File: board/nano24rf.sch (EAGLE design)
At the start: 18 parts

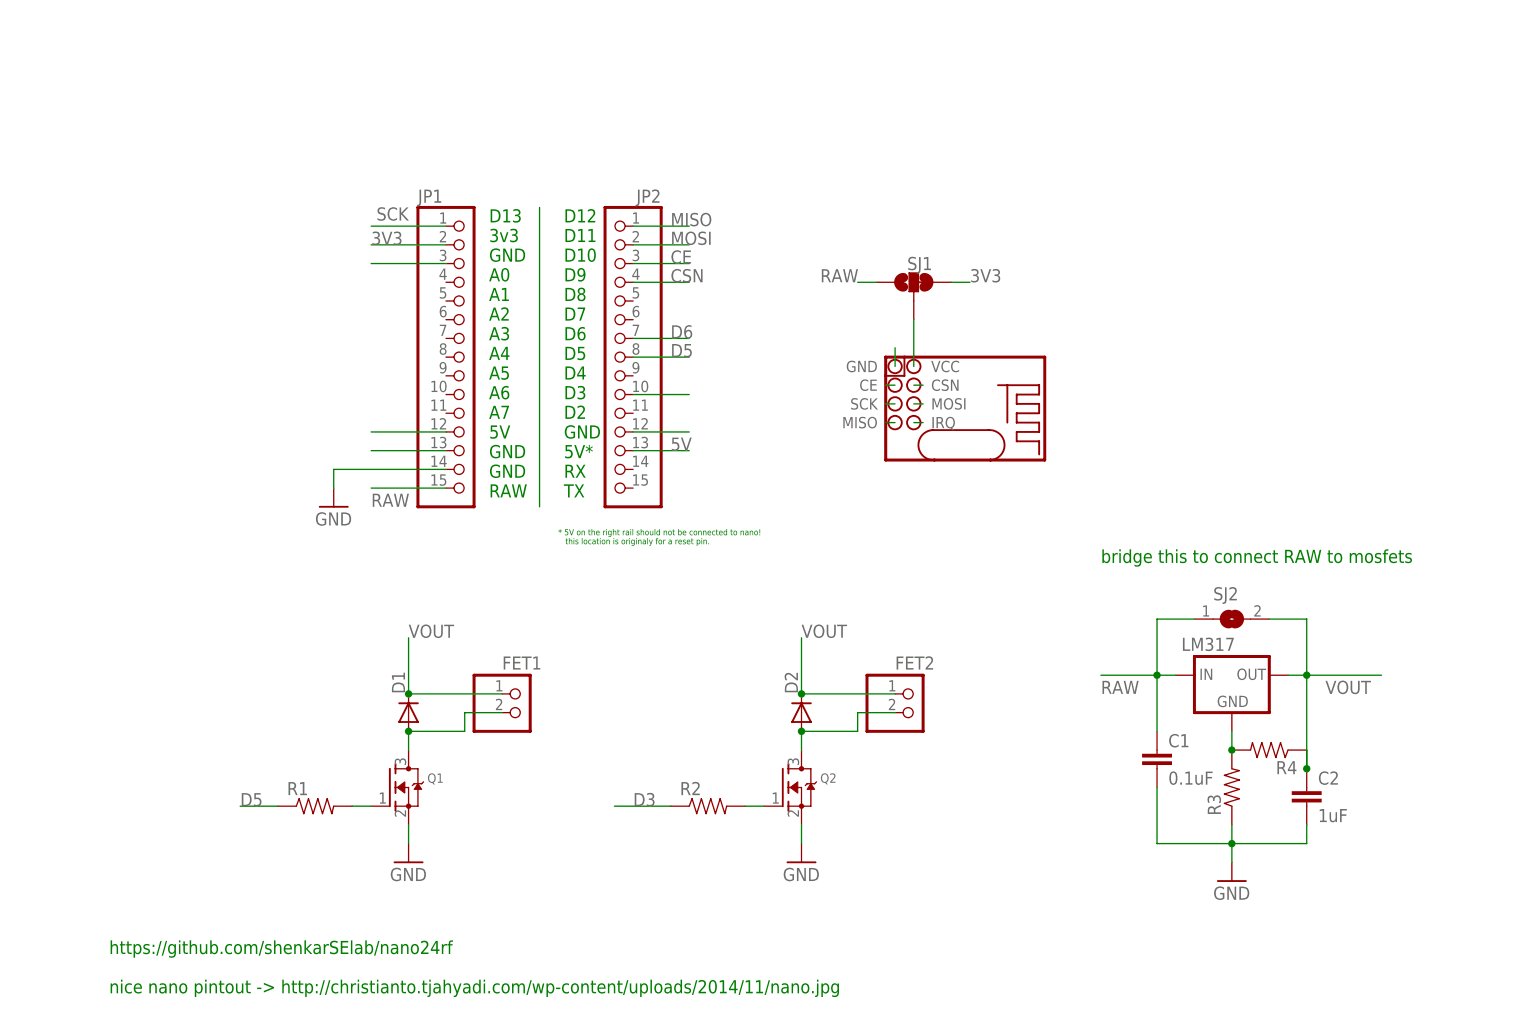
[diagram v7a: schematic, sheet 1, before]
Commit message: removed lm317 and placed msfets on bottom
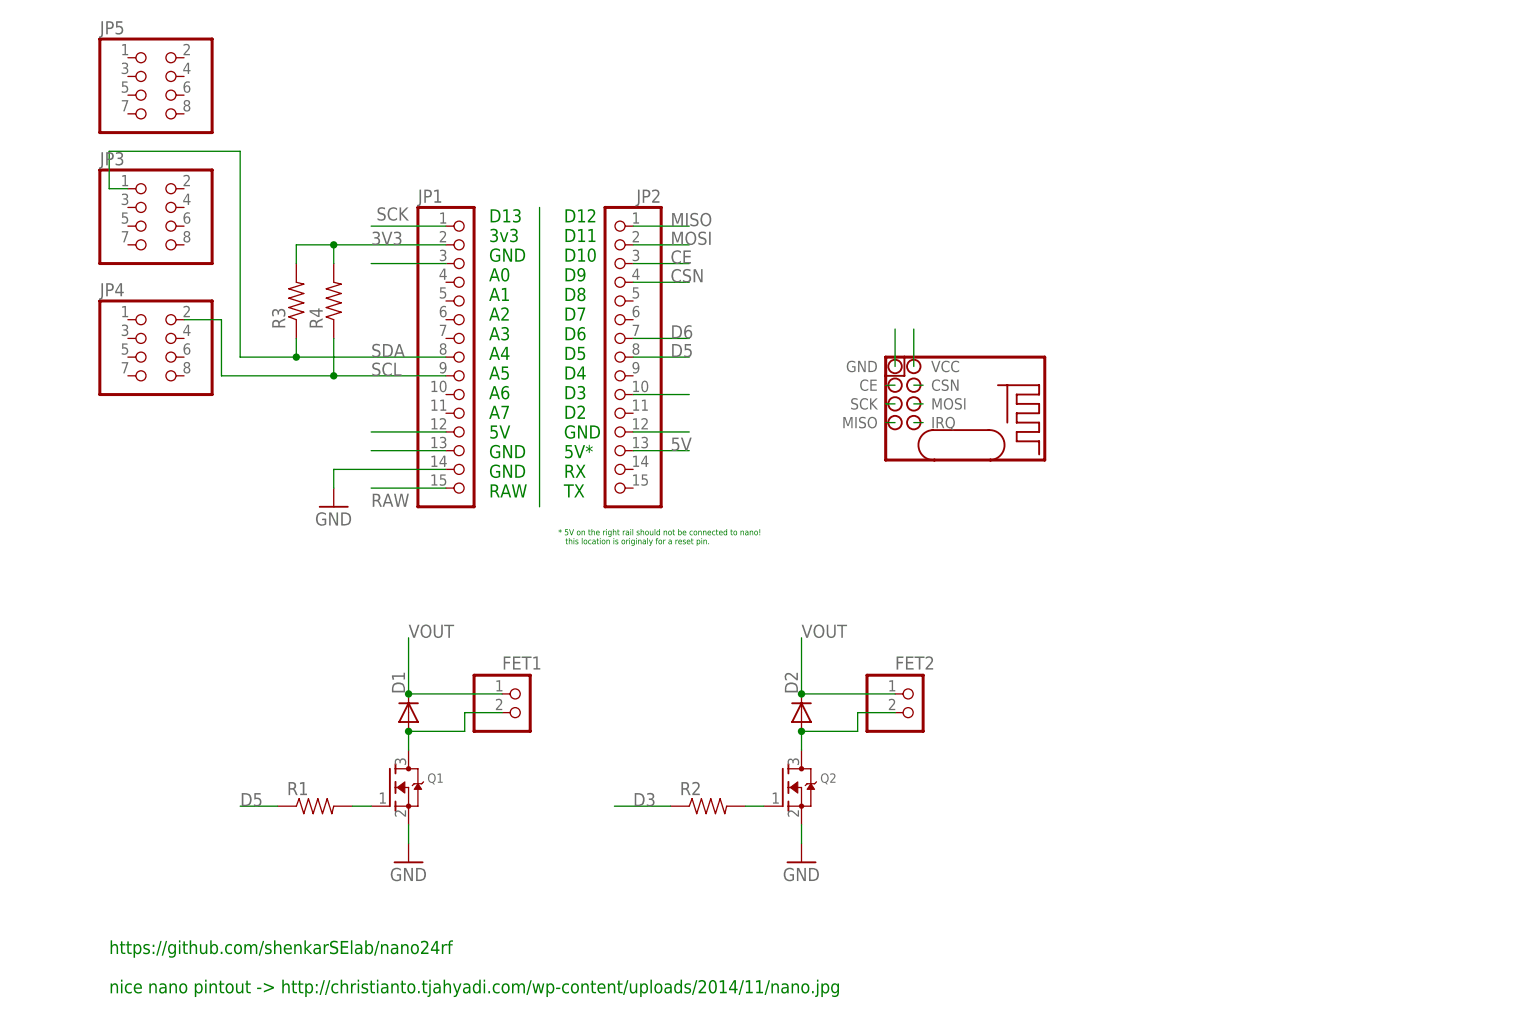
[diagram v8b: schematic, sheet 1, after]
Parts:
- removed C1: 0.1uF, ATTAMI-V0.00:CAP0805
- removed C2: 1uF, ATTAMI-V0.00:CAP0805
- removed LM317: (no value), ATTAMI-V0.00:XXX1117SOT-89
- removed SJ1: JUMPER-PAD-3-2OF3_NC_BY_TRACE_LARGE, ATTAMI-V0.00:JUMPER-PAD-3-2OF3_NC_BY_TRACE_LARGE
- removed SJ2: (no value), microbuilder:SOLDERJUMPERREFLOW
- added JP3, JP4, JP5: (no value), adafruit:PINHD-2X4
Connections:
- removed net N$7: LM317.GND, R3.2, R4.2
- new net SCL: JP1.9, JP4.2, R4.1
- new net SDA: JP1.8, JP3.1, R3.1
- net 3V3: now also R3.2, R4.2; no longer SJ1.2, SJ1.3
- net GND: no longer C1.2, C2.2, R3.1
- net RAW: no longer C1.1, LM317.IN, SJ1.1, SJ2.1
- net VOUT: no longer C2.1, LM317.OUT, R4.1, SJ2.2
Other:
- note removed: "bridge this to connect RAW to mosfets"
- moved on the sheet: R3, R4
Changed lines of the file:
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@@
 <part name="R2" library="ATTAMI-V0.00" deviceset="RESISTOR" device="0805-RES"/>
 <part name="U$5" library="ATTAMI-V0.00" deviceset="GND" device=""/>
-<part name="SJ1" library="ATTAMI-V0.00" deviceset="JUMPER-PAD-3-2OF3_NC_BY_TRACE" device="_LARGE"/>
-<part name="LM317" library="ATTAMI-V0.00" deviceset="XXX1117" device="SOT-89"/>
-<part name="C1" library="ATTAMI-V0.00" deviceset="CAP" device="0805" value="0.1uF"/>
-<part name="C2" library="ATTAMI-V0.00" deviceset="CAP" device="0805" value="1uF"/>
-<part name="U$6" library="ATTAMI-V0.00" deviceset="GND" device=""/>
+<part name="JP1" library="microbuilder" deviceset="HEADER-1X15" device=""/>
+<part name="JP2" library="microbuilder" deviceset="HEADER-1X15" device=""/>
+<part name="JP3" library="adafruit" deviceset="PINHD-2X4" device=""/>
 <part name="R3" library="ATTAMI-V0.00" deviceset="RESISTOR" device="0805-RES"/>
 <part name="R4" library="ATTAMI-V0.00" deviceset="RESISTOR" device="0805-RES"/>
-<part name="JP1" library="microbuilder" deviceset="HEADER-1X15" device=""/>
-<part name="JP2" library="microbuilder" deviceset="HEADER-1X15" device=""/>
-<part name="SJ2" library="microbuilder" deviceset="SOLDERJUMPER" device="REFLOW"/>
+<part name="JP4" library="adafruit" deviceset="PINHD-2X4" device=""/>
+<part name="JP5" library="adafruit" deviceset="PINHD-2X4" device=""/>
 </parts>
 <sheets>
@@
 <text x="58.42" y="22.86" size="0.8128" layer="91">* 5V on the right rail should not be connected to nano!
    this location is originaly for a reset pin. </text>
-<text x="132.08" y="20.32" size="1.778" layer="91">bridge this to connect RAW to mosfets</text>
 </plain>
 <instances>
@@
 <instance part="R2" gate="G$1" x="78.74" y="-12.7"/>
 <instance part="U$5" gate="1" x="27.94" y="27.94"/>
-<instance part="SJ1" gate="G$1" x="106.68" y="58.42" smashed="yes" rot="R90">
-<attribute name="NAME" x="109.22" y="61.849" size="1.778" layer="95" rot="R180"/>
-</instance>
-<instance part="LM317" gate="1" x="149.86" y="5.08" smashed="yes">
-<attribute name="NAME" x="143.002" y="8.382" size="1.778" layer="95"/>
-<attribute name="VALUE" x="152.4" y="-5.08" size="1.778" layer="96"/>
-</instance>
-<instance part="C1" gate="G$1" x="139.7" y="-7.62"/>
-<instance part="C2" gate="G$1" x="160.02" y="-12.7"/>
-<instance part="U$6" gate="1" x="149.86" y="-22.86"/>
-<instance part="R3" gate="G$1" x="149.86" y="-10.16" rot="R90"/>
-<instance part="R4" gate="G$1" x="154.94" y="-5.08" rot="R180"/>
 <instance part="JP1" gate="G$1" x="45.72" y="48.26"/>
 <instance part="JP2" gate="G$1" x="66.04" y="48.26" rot="MR0"/>
-<instance part="SJ2" gate="1" x="149.86" y="12.7"/>
+<instance part="JP3" gate="A" x="2.54" y="66.04"/>
+<instance part="R3" gate="G$1" x="22.86" y="55.88" rot="R90"/>
+<instance part="R4" gate="G$1" x="27.94" y="55.88" rot="R90"/>
+<instance part="JP4" gate="A" x="2.54" y="48.26"/>
+<instance part="JP5" gate="A" x="2.54" y="83.82"/>
 </instances>
 <busses>
@@
 </segment>
 <segment>
-<pinref part="C1" gate="G$1" pin="2"/>
-<pinref part="C2" gate="G$1" pin="2"/>
-<wire x1="139.7" y1="-10.16" x2="139.7" y2="-17.78" width="0.1524" layer="91"/>
-<wire x1="139.7" y1="-17.78" x2="149.86" y2="-17.78" width="0.1524" layer="91"/>
-<wire x1="149.86" y1="-17.78" x2="160.02" y2="-17.78" width="0.1524" layer="91"/>
-<wire x1="160.02" y1="-17.78" x2="160.02" y2="-15.24" width="0.1524" layer="91"/>
-<junction x="149.86" y="-17.78"/>
-<pinref part="U$6" gate="1" pin="GND"/>
-<wire x1="149.86" y1="-15.24" x2="149.86" y2="-17.78" width="0.1524" layer="91"/>
-<wire x1="149.86" y1="-17.78" x2="149.86" y2="-20.32" width="0.1524" layer="91"/>
-<pinref part="R3" gate="G$1" pin="1"/>
-</segment>
-<segment>
 <pinref part="JP1" gate="G$1" pin="14"/>
 <pinref part="U$5" gate="1" pin="GND"/>
@@
 <segment>
 <pinref part="U$2" gate="G$1" pin="GND"/>
-<wire x1="104.14" y1="46.99" x2="104.14" y2="49.53" width="0.1524" layer="91"/>
+<wire x1="104.14" y1="46.99" x2="104.14" y2="52.07" width="0.1524" layer="91"/>
 </segment>
 <segment>
@@
 <net name="RAW" class="0">
 <segment>
-<pinref part="LM317" gate="1" pin="IN"/>
-<pinref part="C1" gate="G$1" pin="1"/>
-<wire x1="142.24" y1="5.08" x2="139.7" y2="5.08" width="0.1524" layer="91"/>
-<wire x1="139.7" y1="5.08" x2="139.7" y2="-2.54" width="0.1524" layer="91"/>
-<wire x1="139.7" y1="5.08" x2="132.08" y2="5.08" width="0.1524" layer="91"/>
-<junction x="139.7" y="5.08"/>
-<label x="132.08" y="2.54" size="1.778" layer="95"/>
-<wire x1="139.7" y1="5.08" x2="139.7" y2="12.7" width="0.1524" layer="91"/>
-<wire x1="139.7" y1="12.7" x2="144.78" y2="12.7" width="0.1524" layer="91"/>
-<pinref part="SJ2" gate="1" pin="1"/>
-</segment>
-<segment>
 <pinref part="JP1" gate="G$1" pin="15"/>
 <wire x1="43.18" y1="30.48" x2="33.02" y2="30.48" width="0.1524" layer="91"/>
 <label x="33.02" y="27.94" size="1.778" layer="95"/>
-</segment>
-<segment>
-<pinref part="SJ1" gate="G$1" pin="1"/>
-<wire x1="101.6" y1="58.42" x2="99.06" y2="58.42" width="0.1524" layer="91"/>
-<label x="93.98" y="58.42" size="1.778" layer="95"/>
 </segment>
 </net>
@@
 <net name="VOUT" class="0">
 <segment>
-<pinref part="LM317" gate="1" pin="OUT"/>
-<pinref part="C2" gate="G$1" pin="1"/>
-<wire x1="157.48" y1="5.08" x2="160.02" y2="5.08" width="0.1524" layer="91"/>
-<wire x1="160.02" y1="5.08" x2="160.02" y2="-7.62" width="0.1524" layer="91"/>
-<wire x1="160.02" y1="5.08" x2="170.18" y2="5.08" width="0.1524" layer="91"/>
-<junction x="160.02" y="5.08"/>
-<pinref part="R4" gate="G$1" pin="1"/>
-<junction x="160.02" y="-7.62"/>
-<wire x1="160.02" y1="-7.62" x2="160.02" y2="-5.08" width="0.1524" layer="91"/>
-<label x="162.56" y="2.54" size="1.778" layer="95"/>
-<wire x1="160.02" y1="5.08" x2="160.02" y2="12.7" width="0.1524" layer="91"/>
-<wire x1="160.02" y1="12.7" x2="154.94" y2="12.7" width="0.1524" layer="91"/>
-<pinref part="SJ2" gate="1" pin="2"/>
-</segment>
-<segment>
 <pinref part="D2" gate="D" pin="C"/>
 <wire x1="91.44" y1="10.16" x2="91.44" y2="2.54" width="0.1524" layer="91"/>
@@
 </segment>
 </net>
-<net name="N$7" class="0">
-<segment>
-<pinref part="LM317" gate="1" pin="GND"/>
+<net name="N$3" class="0">
+<segment>
+<wire x1="55.88" y1="68.58" x2="55.88" y2="27.94" width="0.4064" layer="91"/>
+</segment>
+</net>
+<net name="3V3" class="0">
+<segment>
+<pinref part="JP1" gate="G$1" pin="2"/>
+<label x="33.02" y="63.5" size="1.778" layer="95"/>
 <pinref part="R3" gate="G$1" pin="2"/>
+<wire x1="43.18" y1="63.5" x2="27.94" y2="63.5" width="0.1524" layer="91"/>
+<wire x1="27.94" y1="63.5" x2="22.86" y2="63.5" width="0.1524" layer="91"/>
+<wire x1="22.86" y1="63.5" x2="22.86" y2="60.96" width="0.1524" layer="91"/>
 <pinref part="R4" gate="G$1" pin="2"/>
-<junction x="149.86" y="-5.08"/>
-<wire x1="149.86" y1="-5.08" x2="149.86" y2="-2.54" width="0.1524" layer="91"/>
-</segment>
-</net>
-<net name="N$3" class="0">
-<segment>
-<wire x1="55.88" y1="68.58" x2="55.88" y2="27.94" width="0.4064" layer="91"/>
-</segment>
-</net>
-<net name="3V3" class="0">
-<segment>
-<pinref part="JP1" gate="G$1" pin="2"/>
-<wire x1="43.18" y1="63.5" x2="33.02" y2="63.5" width="0.1524" layer="91"/>
-<label x="33.02" y="63.5" size="1.778" layer="95"/>
+<wire x1="27.94" y1="63.5" x2="27.94" y2="60.96" width="0.1524" layer="91"/>
+<junction x="27.94" y="63.5"/>
 </segment>
 <segment>
 <pinref part="U$2" gate="G$1" pin="VCC"/>
-<wire x1="106.68" y1="46.99" x2="106.68" y2="53.34" width="0.1524" layer="91"/>
-<pinref part="SJ1" gate="G$1" pin="2"/>
-</segment>
-<segment>
-<pinref part="SJ1" gate="G$1" pin="3"/>
-<wire x1="111.76" y1="58.42" x2="114.3" y2="58.42" width="0.1524" layer="91"/>
-<label x="114.3" y="58.42" size="1.778" layer="95"/>
+<wire x1="106.68" y1="46.99" x2="106.68" y2="52.07" width="0.1524" layer="91"/>
 </segment>
 </net>
@@
 </segment>
 </net>
+<net name="SDA" class="0">
+<segment>
+<pinref part="JP1" gate="G$1" pin="8"/>
+<wire x1="43.18" y1="48.26" x2="22.86" y2="48.26" width="0.1524" layer="91"/>
+<label x="33.02" y="48.26" size="1.778" layer="95"/>
+<pinref part="R3" gate="G$1" pin="1"/>
+<wire x1="22.86" y1="48.26" x2="15.24" y2="48.26" width="0.1524" layer="91"/>
+<wire x1="22.86" y1="50.8" x2="22.86" y2="48.26" width="0.1524" layer="91"/>
+<junction x="22.86" y="48.26"/>
+<wire x1="15.24" y1="48.26" x2="15.24" y2="76.2" width="0.1524" layer="91"/>
+<wire x1="15.24" y1="76.2" x2="-2.54" y2="76.2" width="0.1524" layer="91"/>
+<wire x1="-2.54" y1="76.2" x2="-2.54" y2="71.12" width="0.1524" layer="91"/>
+<pinref part="JP3" gate="A" pin="1"/>
+<wire x1="-2.54" y1="71.12" x2="0" y2="71.12" width="0.1524" layer="91"/>
+</segment>
+</net>
+<net name="SCL" class="0">
+<segment>
+<pinref part="R4" gate="G$1" pin="1"/>
+<wire x1="27.94" y1="50.8" x2="27.94" y2="45.72" width="0.1524" layer="91"/>
+<pinref part="JP1" gate="G$1" pin="9"/>
+<wire x1="27.94" y1="45.72" x2="43.18" y2="45.72" width="0.1524" layer="91"/>
+<wire x1="27.94" y1="45.72" x2="12.7" y2="45.72" width="0.1524" layer="91"/>
+<junction x="27.94" y="45.72"/>
+<label x="33.02" y="45.72" size="1.778" layer="95"/>
+<pinref part="JP4" gate="A" pin="2"/>
+<wire x1="7.62" y1="53.34" x2="12.7" y2="53.34" width="0.1524" layer="91"/>
+<wire x1="12.7" y1="53.34" x2="12.7" y2="45.72" width="0.1524" layer="91"/>
+</segment>
+</net>
